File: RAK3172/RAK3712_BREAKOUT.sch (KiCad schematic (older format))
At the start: 3 parts

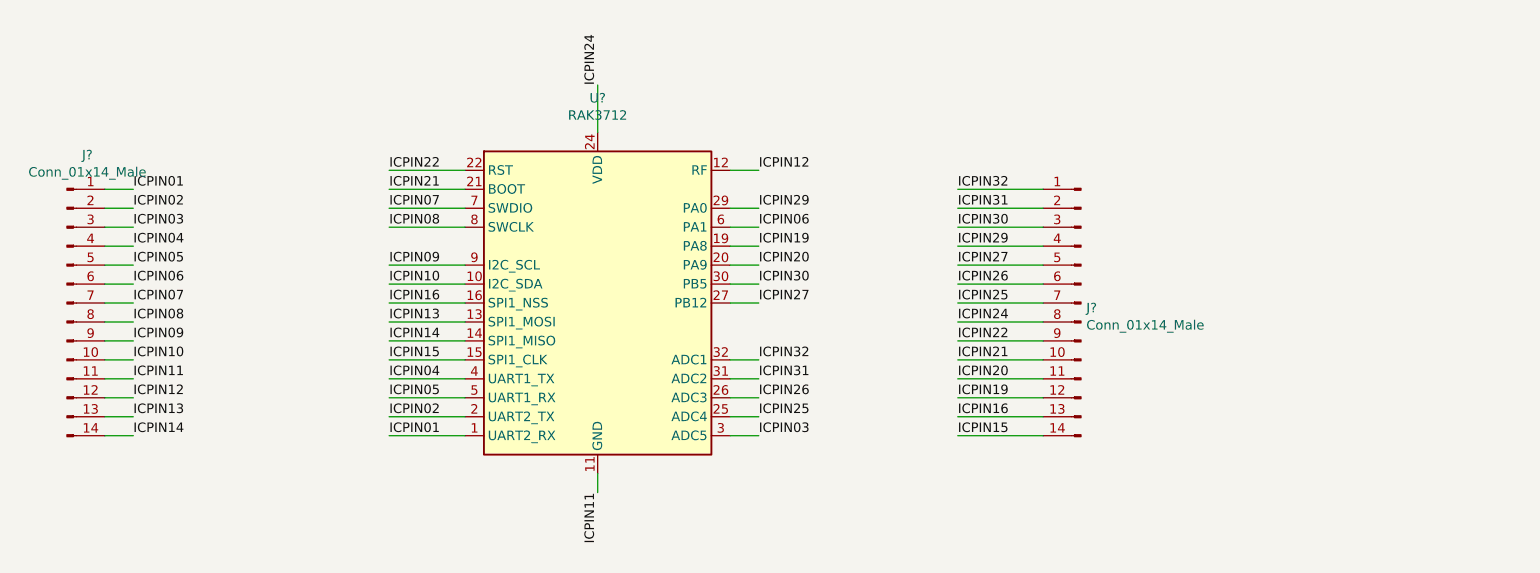
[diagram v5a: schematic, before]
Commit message: foot:(DIL_BREAKOUT_PCB RAK 3712)ready for route
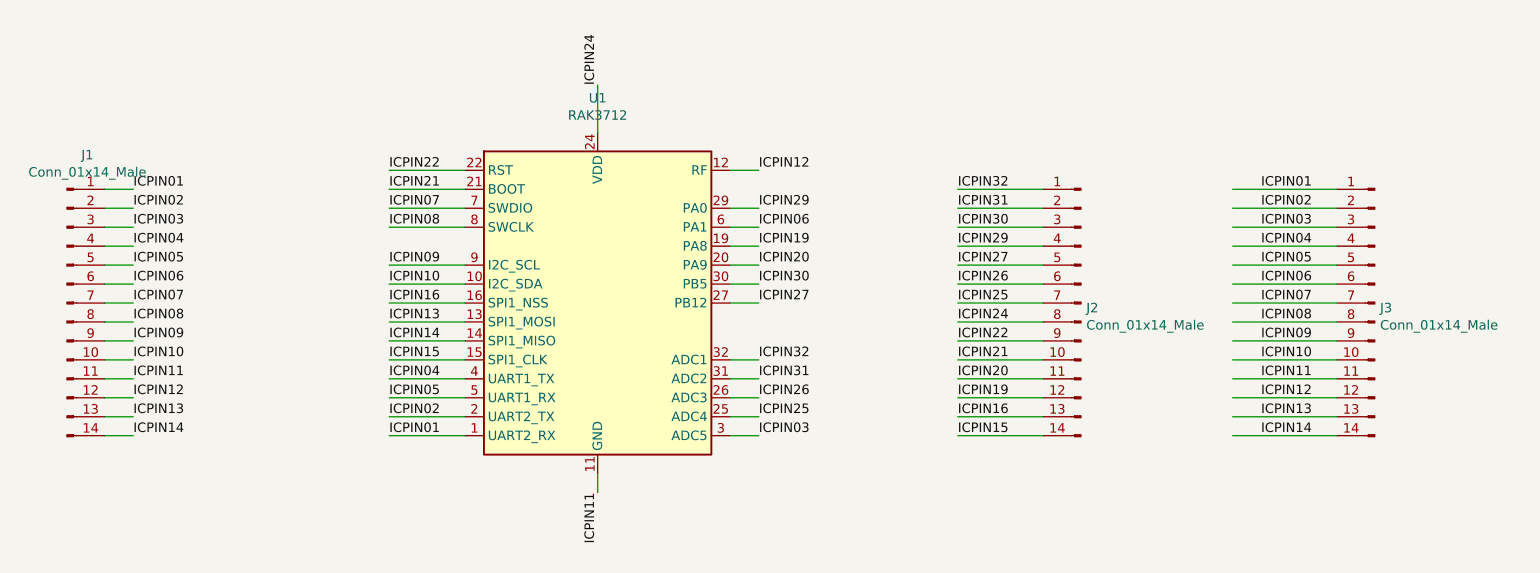
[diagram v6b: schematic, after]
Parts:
- added J3: Conn_01x14_Male, Connector_PinHeader_2.54mm:PinHeader_1x14_P2.54mm_Vertical, symbol Connector:Conn_01x14_Male
- J1, J2: renamed from J?; footprint (none) -> Connector_PinHeader_2.54mm:PinHeader_1x14_P2.54mm_Vertical
- gave numbers to parts that had none: 1
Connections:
- wire segments 56 -> 70
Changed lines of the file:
@@
 ICPIN32
 $Comp
-L RAKWIRELESS:RAK3712 U?
+L RAKWIRELESS:RAK3712 U1
 U 1 1 621FE0F5
 P 5650 2850
-F 0 "U?" H 5650 3931 50  0000 C CNN
+F 0 "U1" H 5650 3931 50  0000 C CNN
 F 1 "RAK3712" H 5650 3840 50  0000 C CNN
 F 2 "RAKWIRELESS:RAK3712" H 5850 3150 50  0001 C CNN
@@
 $EndComp
 $Comp
-L Connector:Conn_01x14_Male J?
+L Connector:Conn_01x14_Male J1
 U 1 1 621F2722
 P 2850 2850
-F 0 "J?" H 2958 3631 50  0000 C CNN
+F 0 "J1" H 2958 3631 50  0000 C CNN
 F 1 "Conn_01x14_Male" H 2958 3540 50  0000 C CNN
-F 2 "" H 2850 2850 50  0001 C CNN
+F 2 "Connector_PinHeader_2.54mm:PinHeader_1x14_P2.54mm_Vertical" H 2850 2850 50  0001 C CNN
 F 3 "~" H 2850 2850 50  0001 C CNN
 	1    2850 2850
@@
 $EndComp
 $Comp
-L Connector:Conn_01x14_Male J?
+L Connector:Conn_01x14_Male J2
 U 1 1 621FB759
 P 8200 2850
-F 0 "J?" H 8172 2824 50  0000 R CNN
+F 0 "J2" H 8172 2824 50  0000 R CNN
 F 1 "Conn_01x14_Male" H 8172 2733 50  0000 R CNN
-F 2 "" H 8200 2850 50  0001 C CNN
+F 2 "Connector_PinHeader_2.54mm:PinHeader_1x14_P2.54mm_Vertical" H 8200 2850 50  0001 C CNN
 F 3 "~" H 8200 2850 50  0001 C CNN
 	1    8200 2850
@@
 Wire Wire Line
 	7550 3550 8000 3550
+$Comp
+L Connector:Conn_01x14_Male J3
+U 1 1 621F6CCC
+P 9750 2850
+F 0 "J3" H 9722 2824 50  0000 R CNN
+F 1 "Conn_01x14_Male" H 9722 2733 50  0000 R CNN
+F 2 "Connector_PinHeader_2.54mm:PinHeader_1x14_P2.54mm_Vertical" H 9750 2850 50  0001 C CNN
+F 3 "~" H 9750 2850 50  0001 C CNN
+	1    9750 2850
+	-1   0    0    -1
+$EndComp
+Text Label 9150 2250 0    50   ~ 0
+ICPIN01
+Text Label 9150 2350 0    50   ~ 0
+ICPIN02
+Text Label 9150 2450 0    50   ~ 0
+ICPIN03
+Text Label 9150 2550 0    50   ~ 0
+ICPIN04
+Text Label 9150 2650 0    50   ~ 0
+ICPIN05
+Text Label 9150 2750 0    50   ~ 0
+ICPIN06
+Text Label 9150 2850 0    50   ~ 0
+ICPIN07
+Text Label 9150 2950 0    50   ~ 0
+ICPIN08
+Text Label 9150 3050 0    50   ~ 0
+ICPIN09
+Text Label 9150 3150 0    50   ~ 0
+ICPIN10
+Text Label 9150 3250 0    50   ~ 0
+ICPIN11
+Text Label 9150 3350 0    50   ~ 0
+ICPIN12
+Text Label 9150 3450 0    50   ~ 0
+ICPIN13
+Text Label 9150 3550 0    50   ~ 0
+ICPIN14
+Wire Wire Line
+	9000 2250 9550 2250
+Wire Wire Line
+	9000 2350 9550 2350
+Wire Wire Line
+	9000 2450 9550 2450
+Wire Wire Line
+	9000 2550 9550 2550
+Wire Wire Line
+	9000 2650 9550 2650
+Wire Wire Line
+	9000 2750 9550 2750
+Wire Wire Line
+	9000 2850 9550 2850
+Wire Wire Line
+	9000 2950 9550 2950
+Wire Wire Line
+	9000 3050 9550 3050
+Wire Wire Line
+	9000 3150 9550 3150
+Wire Wire Line
+	9000 3250 9550 3250
+Wire Wire Line
+	9000 3350 9550 3350
+Wire Wire Line
+	9000 3450 9550 3450
+Wire Wire Line
+	9000 3550 9550 3550
 $EndSCHEMATC
